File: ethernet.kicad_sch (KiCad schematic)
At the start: 33 parts, among them J4 RJ45, U21 KSZ8851-16MLL, Y3 25MHz

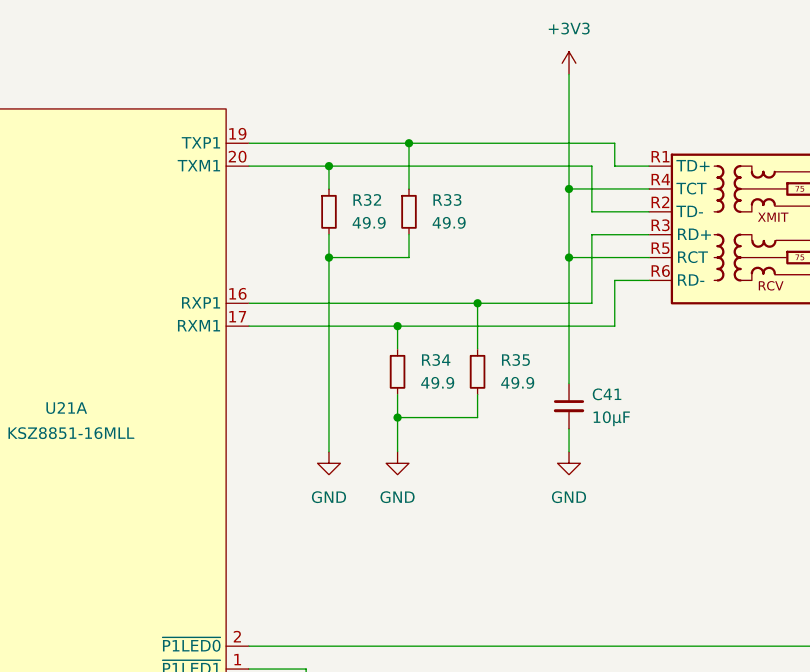
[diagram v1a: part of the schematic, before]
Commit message: update value of 49.9 ethernet resistors to reflect 1/4 W
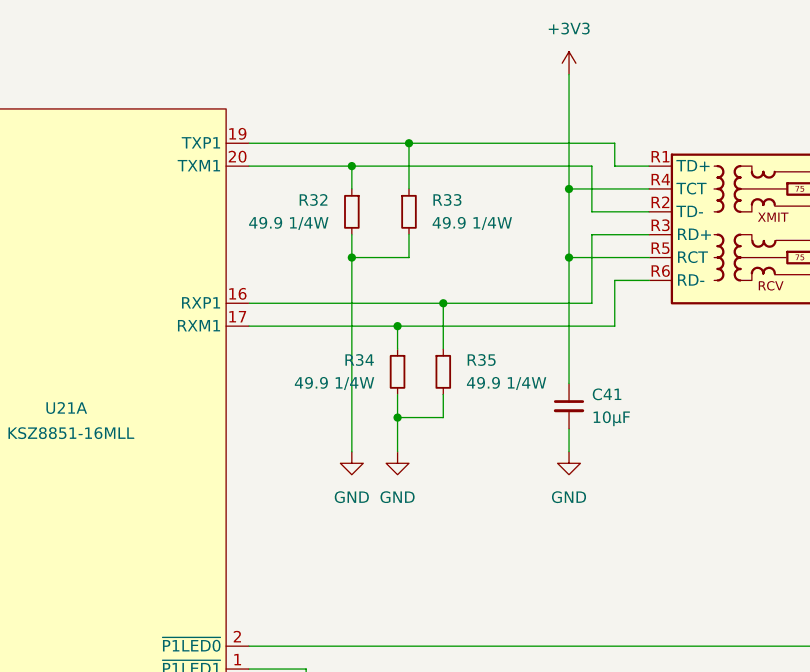
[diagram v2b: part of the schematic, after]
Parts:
- R32, R33, R34, R35: value 49.9 -> 49.9 1/4W
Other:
- moved on the sheet: R32, R35
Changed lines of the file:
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@@
 	)
 	(junction
-		(at 193.04 212.09)
+		(at 154.94 43.18)
 		(diameter 0)
 		(color 0 0 0 0)
 	)
 	(junction
-		(at 154.94 43.18)
+		(at 110.49 218.44)
 		(diameter 0)
 		(color 0 0 0 0)
 	)
 	(junction
-		(at 110.49 218.44)
+		(at 189.23 212.09)
 		(diameter 0)
 		(color 0 0 0 0)
@@
 	)
 	(junction
+		(at 179.07 196.85)
+		(diameter 0)
+		(color 0 0 0 0)
+	)
+	(junction
 		(at 120.65 219.71)
 		(diameter 0)
@@
 	)
 	(junction
-		(at 176.53 207.01)
-		(diameter 0)
-		(color 0 0 0 0)
-	)
-	(junction
 		(at 203.2 207.01)
 		(diameter 0)
@@
 	)
 	(junction
-		(at 176.53 196.85)
-		(diameter 0)
-		(color 0 0 0 0)
-	)
-	(junction
 		(at 114.3 35.56)
 		(diameter 0)
@@
 	)
 	(junction
+		(at 179.07 207.01)
+		(diameter 0)
+		(color 0 0 0 0)
+	)
+	(junction
 		(at 120.65 217.17)
 		(diameter 0)
@@
 	(wire
 		(pts
+			(xy 189.23 212.09) (xy 205.74 212.09)
+		)
+		(stroke
+			(width 0)
+			(type default)
+		)
+	)
+	(wire
+		(pts
 			(xy 135.89 43.18) (xy 135.89 46.99)
 		)
@@
 	(wire
 		(pts
+			(xy 179.07 207.01) (xy 185.42 207.01)
+		)
+		(stroke
+			(width 0)
+			(type default)
+		)
+	)
+	(wire
+		(pts
 			(xy 120.65 227.33) (xy 120.65 224.79)
 		)
@@
 	(wire
 		(pts
-			(xy 167.64 212.09) (xy 193.04 212.09)
+			(xy 167.64 212.09) (xy 189.23 212.09)
 		)
 		(stroke
@@
 	(wire
 		(pts
+			(xy 179.07 196.85) (xy 205.74 196.85)
+		)
+		(stroke
+			(width 0)
+			(type default)
+		)
+	)
+	(wire
+		(pts
 			(xy 275.59 73.66) (xy 288.29 73.66)
 		)
@@
 	(wire
 		(pts
-			(xy 193.04 217.17) (xy 193.04 212.09)
+			(xy 189.23 217.17) (xy 189.23 212.09)
 		)
 		(stroke
@@
 	(wire
 		(pts
-			(xy 176.53 207.01) (xy 176.53 228.6)
+			(xy 179.07 207.01) (xy 179.07 228.6)
 		)
 		(stroke
@@
 	(wire
 		(pts
-			(xy 193.04 212.09) (xy 205.74 212.09)
-		)
-		(stroke
-			(width 0)
-			(type default)
-		)
-	)
-	(wire
-		(pts
 			(xy 154.94 35.56) (xy 154.94 43.18)
 		)
@@
 	(wire
 		(pts
-			(xy 184.15 224.79) (xy 193.04 224.79)
+			(xy 184.15 224.79) (xy 189.23 224.79)
 		)
 		(stroke
@@
 	(wire
 		(pts
-			(xy 176.53 204.47) (xy 176.53 207.01)
+			(xy 179.07 204.47) (xy 179.07 207.01)
 		)
 		(stroke
@@
 	(wire
 		(pts
-			(xy 176.53 196.85) (xy 205.74 196.85)
-		)
-		(stroke
-			(width 0)
-			(type default)
-		)
-	)
-	(wire
-		(pts
 			(xy 203.2 199.39) (xy 203.2 207.01)
 		)
@@
 	(wire
 		(pts
-			(xy 176.53 207.01) (xy 185.42 207.01)
-		)
-		(stroke
-			(width 0)
-			(type default)
-		)
-	)
-	(wire
-		(pts
 			(xy 275.59 60.96) (xy 278.13 60.96)
 		)
@@
 	(wire
 		(pts
-			(xy 193.04 224.79) (xy 193.04 222.25)
+			(xy 189.23 224.79) (xy 189.23 222.25)
 		)
 		(stroke
@@
 	(wire
 		(pts
-			(xy 176.53 196.85) (xy 167.64 196.85)
+			(xy 167.64 196.85) (xy 179.07 196.85)
 		)
 		(stroke
@@
 	(wire
 		(pts
-			(xy 176.53 199.39) (xy 176.53 196.85)
+			(xy 179.07 199.39) (xy 179.07 196.85)
 		)
 		(stroke
@@
 		(lib_id "Device:R_Small")
 		(at 184.15 219.71 0)
+		(mirror y)
 		(unit 1)
 		(exclude_from_sim no)
@@
 		(on_board yes)
 		(dnp no)
-		(fields_autoplaced yes)
 		(property "Reference" "R34"
-			(at 186.69 218.4399 0)
+			(at 181.61 218.4399 0)
 			(effects
 				(font
@@
 			)
 		)
-		(property "Value" "49.9"
-			(at 186.69 220.9799 0)
+		(property "Value" "49.9 1/4W"
+			(at 181.61 220.9799 0)
 			(effects
 				(font
@@
 			)
 		)
-		(property "Value" "49.9"
+		(property "Value" "49.9 1/4W"
 			(at 187.96 203.1999 0)
 			(effects
@@
 	(symbol
 		(lib_id "Device:R_Small")
-		(at 193.04 219.71 0)
+		(at 189.23 219.71 0)
 		(unit 1)
 		(exclude_from_sim no)
@@
 		(fields_autoplaced yes)
 		(property "Reference" "R35"
-			(at 195.58 218.4399 0)
+			(at 191.77 218.4399 0)
 			(effects
 				(font
@@
 			)
 		)
-		(property "Value" "49.9"
-			(at 195.58 220.9799 0)
+		(property "Value" "49.9 1/4W"
+			(at 191.77 220.9799 0)
 			(effects
 				(font
@@
 		)
 		(property "Footprint" "Resistor_SMD:R_0402_1005Metric"
-			(at 193.04 219.71 0)
+			(at 189.23 219.71 0)
 			(effects
 				(font
@@
 		)
 		(property "Datasheet" "~"
-			(at 193.04 219.71 0)
+			(at 189.23 219.71 0)
 			(effects
 				(font
@@
 		)
 		(property "Description" "Resistor, small symbol"
-			(at 193.04 219.71 0)
+			(at 189.23 219.71 0)
 			(effects
 				(font
@@
 	(symbol
 		(lib_id "power:GND")
-		(at 176.53 228.6 0)
+		(at 179.07 228.6 0)
 		(unit 1)
 		(exclude_from_sim no)
@@
 		(fields_autoplaced yes)
 		(property "Reference" "#PWR0123"
-			(at 176.53 234.95 0)
+			(at 179.07 234.95 0)
 			(effects
 				(font
@@
 		)
 		(property "Value" "GND"
-			(at 176.53 233.68 0)
+			(at 179.07 233.68 0)
 			(effects
 				(font
@@
 		)
 		(property "Footprint" ""
-			(at 176.53 228.6 0)
+			(at 179.07 228.6 0)
 			(effects
 				(font
@@
 		)
 		(property "Datasheet" ""
-			(at 176.53 228.6 0)
+			(at 179.07 228.6 0)
 			(effects
 				(font
@@
 		)
 		(property "Description" "Power symbol creates a global label with name \"GND\" , ground"
-			(at 176.53 228.6 0)
+			(at 179.07 228.6 0)
 			(effects
 				(font
@@
 	(symbol
 		(lib_id "Device:R_Small")
-		(at 176.53 201.93 0)
+		(at 179.07 201.93 0)
+		(mirror y)
 		(unit 1)
 		(exclude_from_sim no)
@@
 		(on_board yes)
 		(dnp no)
-		(fields_autoplaced yes)
 		(property "Reference" "R32"
-			(at 179.07 200.6599 0)
+			(at 176.53 200.6599 0)
 			(effects
 				(font
@@
 			)
 		)
-		(property "Value" "49.9"
-			(at 179.07 203.1999 0)
+		(property "Value" "49.9 1/4W"
+			(at 176.53 203.1999 0)
 			(effects
 				(font
@@
 		)
 		(property "Footprint" "Resistor_SMD:R_0402_1005Metric"
-			(at 176.53 201.93 0)
+			(at 179.07 201.93 0)
 			(effects
 				(font
@@
 		)
 		(property "Datasheet" "~"
-			(at 176.53 201.93 0)
+			(at 179.07 201.93 0)
 			(effects
 				(font
@@
 		)
 		(property "Description" "Resistor, small symbol"
-			(at 176.53 201.93 0)
+			(at 179.07 201.93 0)
 			(effects
 				(font

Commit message: fix address decoding
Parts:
- C40, C41: LCSC (none) -> C2909425
- C42, C43: LCSC (none) -> C2183219
- C44, C45, C46, C48, C49, C51, C52, C54: LCSC (none) -> C466613
- C47, C50, C53: LCSC (none) -> C2226854
- C55: LCSC (none) -> C327025
- D10, D11: LCSC (none) -> C2902912
- FB1, FB2, FB3: LCSC (none) -> C108308
- R30: LCSC (none) -> C139047
- R31: LCSC (none) -> C375970
- R32, R33, R34, R35: value 49.9 1/4W -> 49.9 1/2W; footprint Resistor_SMD:R_0402_1005Metric -> Resistor_SMD:R_0805_2012Metric; LCSC (none) -> C4088942
- R36, R38: LCSC (none) -> C453594
- R37: LCSC (none) -> C25889
- U21: LCSC (none) -> C633713
- Y3: LCSC (none) -> C7294571

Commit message: add rev4 gerbers, bom files
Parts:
- D10, D11: value 1N4148 -> 1N4148 etc
- FB1, FB2, FB3: value MMZ1005D330C -> 330 @ 100
- J4: value RJ45 -> RJ45 DNP
- R32, R33, R34, R35: value 49.9 1/2W -> 49.9 1/4W+
- Y3: Part ECS-250-18-33-JGN-TR3 -> (none)
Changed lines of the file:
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@@
 			)
 		)
-		(property "Value" "49.9 1/2W"
+		(property "Value" "49.9 1/4W+"
 			(at 181.61 220.9799 0)
 			(effects
@@
 			)
 		)
-		(property "Value" "49.9 1/2W"
+		(property "Value" "49.9 1/4W+"
 			(at 187.96 203.1999 0)
 			(effects
@@
 			)
 		)
-		(property "Value" "49.9 1/2W"
+		(property "Value" "49.9 1/4W+"
 			(at 191.77 220.9799 0)
 			(effects
@@
 			)
 		)
-		(property "Value" "MMZ1005D330C"
+		(property "Value" "330 @ 100"
 			(at 179.07 49.568 0)
 			(effects
@@
 			)
 		)
-		(property "Value" "MMZ1005D330C"
+		(property "Value" "330 @ 100"
 			(at 116.84 30.518 0)
 			(effects
@@
 			)
 		)
-		(property "Value" "1N4148"
+		(property "Value" "1N4148 etc"
 			(at 101.6 85.09 0)
 			(effects
@@
 			)
 		)
-		(property "Value" "49.9 1/2W"
+		(property "Value" "49.9 1/4W+"
 			(at 176.53 203.1999 0)
 			(effects
@@
 			)
 		)
-		(property "Part" "ECS-250-18-33-JGN-TR3"
+		(property "Part" ""
 			(at 229.87 134.112 90)
 			(effects
@@
 			)
 		)
-		(property "Value" "RJ45"
+		(property "Value" "RJ45 DNP"
 			(at 233.68 193.04 0)
 			(effects
@@
 			)
 		)
-		(property "Value" "MMZ1005D330C"
+		(property "Value" "330 @ 100"
 			(at 280.7081 57.15 90)
 			(effects
@@
 			)
 		)
-		(property "Value" "1N4148"
+		(property "Value" "1N4148 etc"
 			(at 114.3 82.5499 90)
 			(effects

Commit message: various changes, add LCSC part #s
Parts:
- C40, C41: value 10µF -> 10µF 16V; LCSC C2909425 -> C109457
- C42, C43: LCSC C2183219 -> C1852854
- C44, C45, C46, C48, C49, C51, C52, C54: LCSC C466613 -> C3012376
- C47, C50, C53: LCSC C2226854 -> C84718
- J4: value RJ45 DNP -> RJ45
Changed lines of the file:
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@@
 			)
 		)
-		(property "LCSC" "C466613"
+		(property "LCSC" "C3012376"
 			(at 135.89 49.53 0)
 			(effects
@@
 			)
 		)
-		(property "LCSC" "C466613"
+		(property "LCSC" "C3012376"
 			(at 146.05 49.53 0)
 			(effects
@@
 			)
 		)
-		(property "LCSC" "C466613"
+		(property "LCSC" "C3012376"
 			(at 300.99 67.31 0)
 			(effects
@@
 			)
 		)
-		(property "LCSC" "C2226854"
+		(property "LCSC" "C84718"
 			(at 288.29 67.31 0)
 			(effects
@@
 			)
 		)
-		(property "LCSC" "C2183219"
+		(property "LCSC" "C1852854"
 			(at 193.04 151.13 0)
 			(effects
@@
 			)
 		)
-		(property "LCSC" "C466613"
+		(property "LCSC" "C3012376"
 			(at 275.59 67.31 0)
 			(effects
@@
 			)
 		)
-		(property "LCSC" "C2226854"
+		(property "LCSC" "C84718"
 			(at 114.3 49.53 0)
 			(effects
@@
 			)
 		)
-		(property "LCSC" "C466613"
+		(property "LCSC" "C3012376"
 			(at 265.43 67.31 0)
 			(effects
@@
 			)
 		)
-		(property "LCSC" "C2226854"
+		(property "LCSC" "C84718"
 			(at 252.73 67.31 0)
 			(effects
@@
 			)
 		)
-		(property "Value" "10µF"
+		(property "Value" "10µF 16V"
 			(at 205.74 224.7962 0)
 			(effects
@@
 			)
 		)
-		(property "LCSC" "C2909425"
+		(property "LCSC" "C109457"
 			(at 203.2 223.52 0)
 			(effects
@@
 			)
 		)
-		(property "LCSC" "C466613"
+		(property "LCSC" "C3012376"
 			(at 184.15 60.96 0)
 			(effects
@@
 			)
 		)
-		(property "LCSC" "C466613"
+		(property "LCSC" "C3012376"
 			(at 125.73 49.53 0)
 			(effects
@@
 			)
 		)
-		(property "LCSC" "C2183219"
+		(property "LCSC" "C1852854"
 			(at 203.2 138.43 0)
 			(effects
@@
 			)
 		)
-		(property "LCSC" "C466613"
+		(property "LCSC" "C3012376"
 			(at 194.31 60.96 0)
 			(effects
@@
 			)
 		)
-		(property "Value" "10µF"
+		(property "Value" "10µF 16V"
 			(at 114.3 96.5262 0)
 			(effects
@@
 			)
 		)
-		(property "LCSC" "C2909425"
+		(property "LCSC" "C109457"
 			(at 111.76 95.25 0)
 			(effects
@@
 			)
 		)
-		(property "Value" "RJ45 DNP"
+		(property "Value" "RJ45"
 			(at 233.68 193.04 0)
 			(effects

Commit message: fix a few bugs
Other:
- title: (none) -> Toy32k
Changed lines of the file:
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@@
 	(paper "A3")
 	(title_block
-		(date "2024-08-10")
-		(rev "Rev 4")
+		(title "Toy32k")
+		(date "2024-08-16")
+		(rev "Rev 5")
 	)
 	(junction
